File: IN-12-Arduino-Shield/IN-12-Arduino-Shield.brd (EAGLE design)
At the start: 100 x 67.3 mm, 21 parts, among them T1 IN-12, T2 IN-12, T3 IN-12, T4 IN-12, U1 K155ID1, U2 K155ID1, U3 K155ID1, U4 K155ID1, U5 ARDUINOR3-DIMENSION

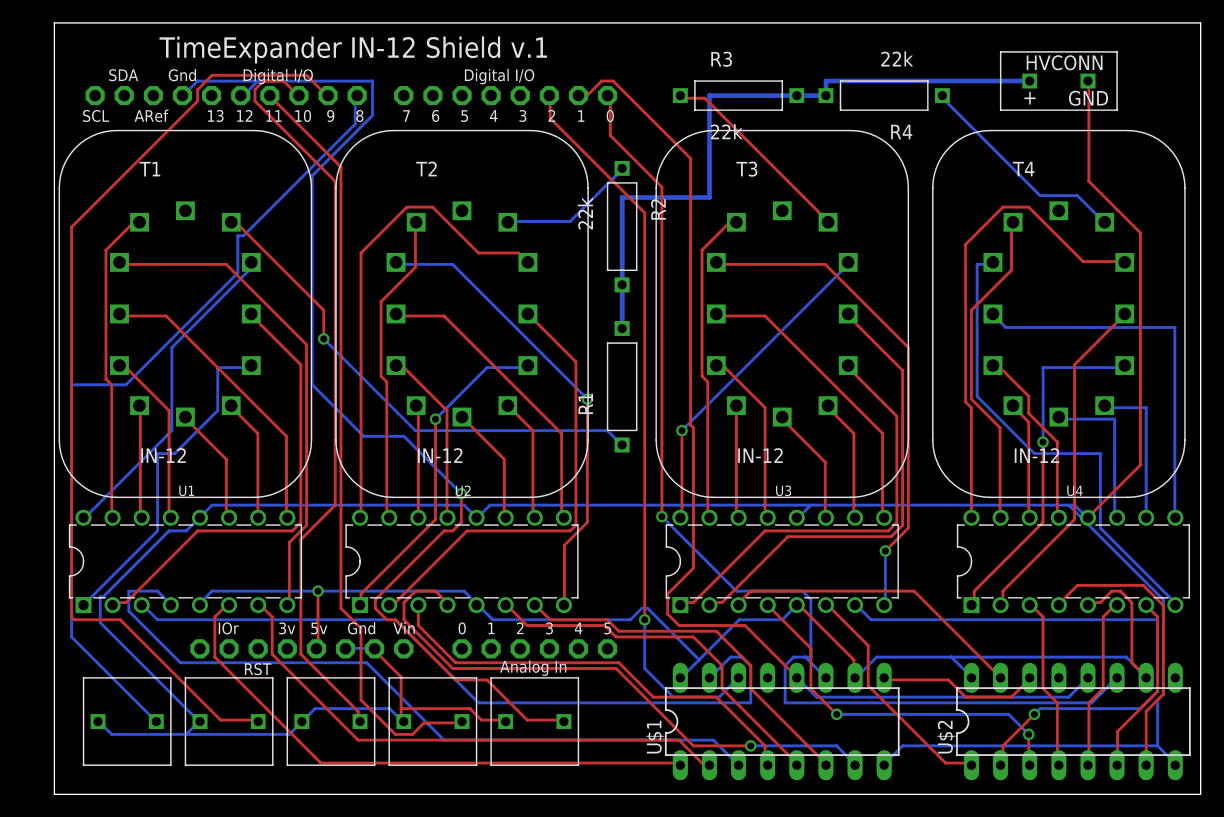
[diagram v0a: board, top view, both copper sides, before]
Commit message: Fixed tube orientation. Added firmware example code.
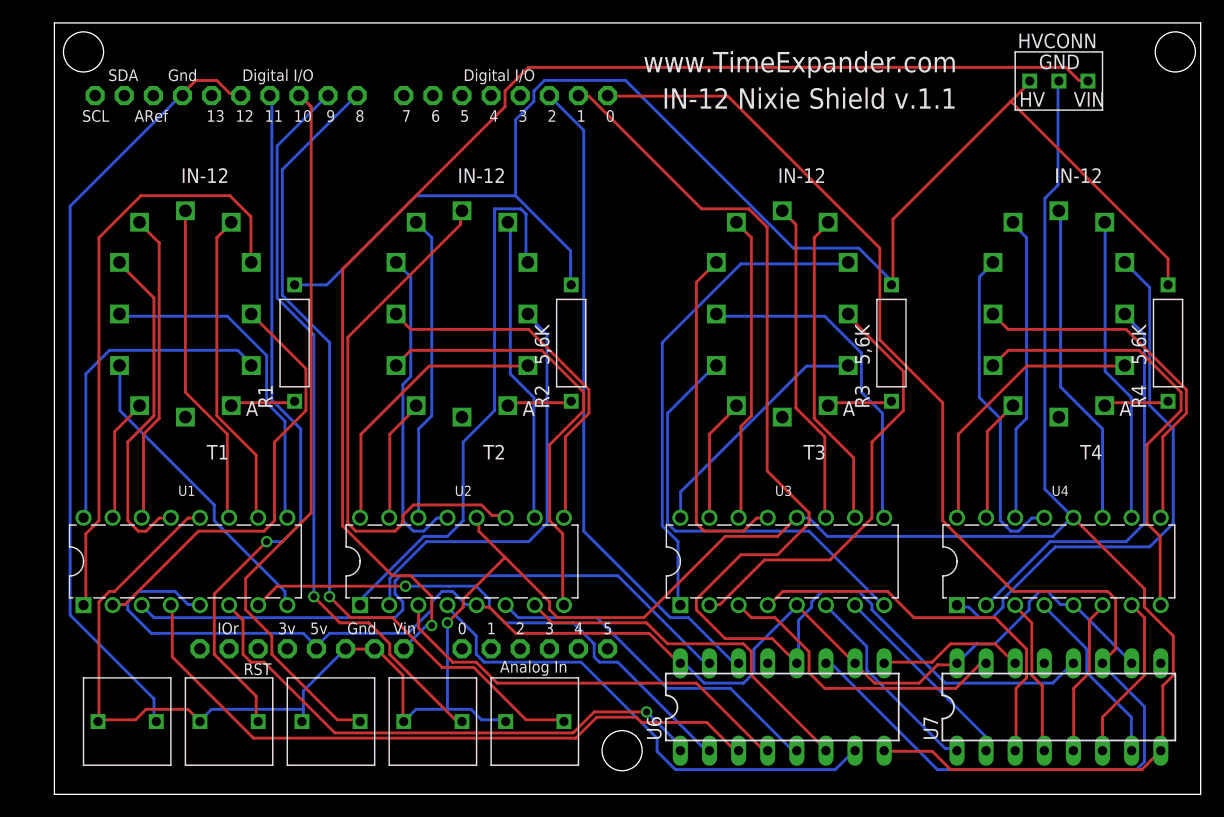
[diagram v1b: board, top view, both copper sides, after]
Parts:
- removed U$1, U$2: 74HC595, TimeExpander:DIL16
- added U6, U7: 74HC595, TimeExpander:DIL16
- R1, R2, R3, R4: value 22k -> 5,6K
- U5: value ARDUINOR3-DIMENSION -> ARDUINOR3; device TimeExpander:ARDUINOR3 -> TimeExpander:ARDUINOR3_NO_OUTLINE
- moved U$3 35.6 mm to (8.89, 7.62)
- moved U$4 35.6 mm to (44.5, 7.62)
- moved R4 33.1 mm to (97.2, 35.6), turned to 90 degrees
- moved R3 32.4 mm to (73.0, 35.6), turned to 90 degrees
- moved R1 28.8 mm to (21.0, 35.6)
- moved R2 20.8 mm to (45.1, 35.6), turned to 90 degrees
- moved U$5 17.8 mm to (35.6, 7.62)
- moved U$7 17.8 mm to (17.8, 7.62)
- moved U4 1.27 mm to (87.6, 21.6)
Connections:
- removed net VIN: U5.VIN
- new net N$55: HVCONN.VIN, U5.VIN
- net +5V: now also U6.10, U6.16, U7.10, U7.16; no longer U$1.10, U$1.16, U$2.10, U$2.16
- net GND: now also U6.8, U7.8; no longer U$1.8, U$2.8
- net N$45: now also U6.13; no longer U$1.13
- net N$46: now also U7.13; no longer U$2.13
- net N$49: now also U6.11, U7.11; no longer U$1.11, U$2.11
- net N$50: now also U6.12, U7.12; no longer U$1.12, U$2.12
- net N$51: now also U6.14; no longer U$1.14
- net N$67: now also U6.15; no longer U$1.15
- net N$68: now also U6.1; no longer U$1.1
- net N$69: now also U6.2; no longer U$1.2
- net N$70: now also U6.3; no longer U$1.3
- net N$71: now also U6.4; no longer U$1.4
- net N$72: now also U6.5; no longer U$1.5
- net N$73: now also U6.6; no longer U$1.6
- net N$74: now also U6.7; no longer U$1.7
- net N$75: now also U7.15; no longer U$2.15
- net N$76: now also U7.1; no longer U$2.1
- net N$77: now also U7.2; no longer U$2.2
- net N$78: now also U7.3; no longer U$2.3
- net N$79: now also U7.4; no longer U$2.4
- net N$80: now also U7.5; no longer U$2.5
- net N$81: now also U7.6; no longer U$2.6
- net N$82: now also U7.7; no longer U$2.7
- net N$91: now also U6.9, U7.14; no longer U$1.9, U$2.14
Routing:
- net N$55: track 0.00 -> 112.1 mm, vias 0 -> 1
- net +24V: track 57.2 -> 125.9 mm
- net N$11: track 43.7 -> 5.67 mm, vias 1 -> 0
- net N$15: track 10.4 -> 47.4 mm
- net N$77: track 50.4 -> 17.4 mm, vias 1 -> 0
- net N$54: track 98.8 -> 68.2 mm, vias 1 -> 0
- net N$49: track 97.9 -> 121.3 mm, vias 1 -> 0
- net N$2: track 29.5 -> 52.2 mm
- net N$13: track 29.0 -> 47.9 mm, vias 1 -> 0
- net N$52: track 83.3 -> 64.9 mm, vias 0 -> 1
- net N$26: track 10.3 -> 28.3 mm
- net N$4: track 10.4 -> 28.3 mm
- net N$42: track 28.3 -> 10.7 mm
- net N$5: track 9.85 -> 27.1 mm
- net N$35: track 30.5 -> 47.7 mm, vias 1 -> 0
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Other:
- board text added: "IN-12 Nixie Shield v.1.1"
- board text added: "www.TimeExpander.com"
- board text removed: "TimeExpander IN-12 Shield v.1"
